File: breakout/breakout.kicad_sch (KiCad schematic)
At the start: 141 parts, among them J1 M20-9982046, J10 B3B-XH-A, J11 B3B-XH-A, J12 B3B-XH-A, J4 B3B-XH-A, J5 B3B-XH-A, J6 B2B-XH-A, J7 B3B-XH-A, J8 B3B-XH-A, J9 B3B-XH-A, Q1 AO3401A, U1 74LVC32APW,118, U10 MCP251863T-E/SS, U11 MCP251863T-E/SS, U12 MCP251863T-E/SS, U13 MCP251863T-E/SS, U14 MCP251863T-E/SS, U15 MCP251863T-E/SS, U16 MCP251863T-E/SS, U2 74LVC04AT14-13, U3 TLV75533PDBVR, U4 74AHC30PW,118, U5 74LVC32APW,118, U9 MCP251863T-E/SS, Y1 ABM8G-40.000MHZ-18-D2Y-T, Y2 ABM8G-40.000MHZ-18-D2Y-T, Y3 ABM8G-40.000MHZ-18-D2Y-T, Y4 ABM8G-40.000MHZ-18-D2Y-T, Y5 ABM8G-40.000MHZ-18-D2Y-T, Y6 ABM8G-40.000MHZ-18-D2Y-T, Y7 ABM8G-40.000MHZ-18-D2Y-T, Y8 ABM8G-40.000MHZ-18-D2Y-T

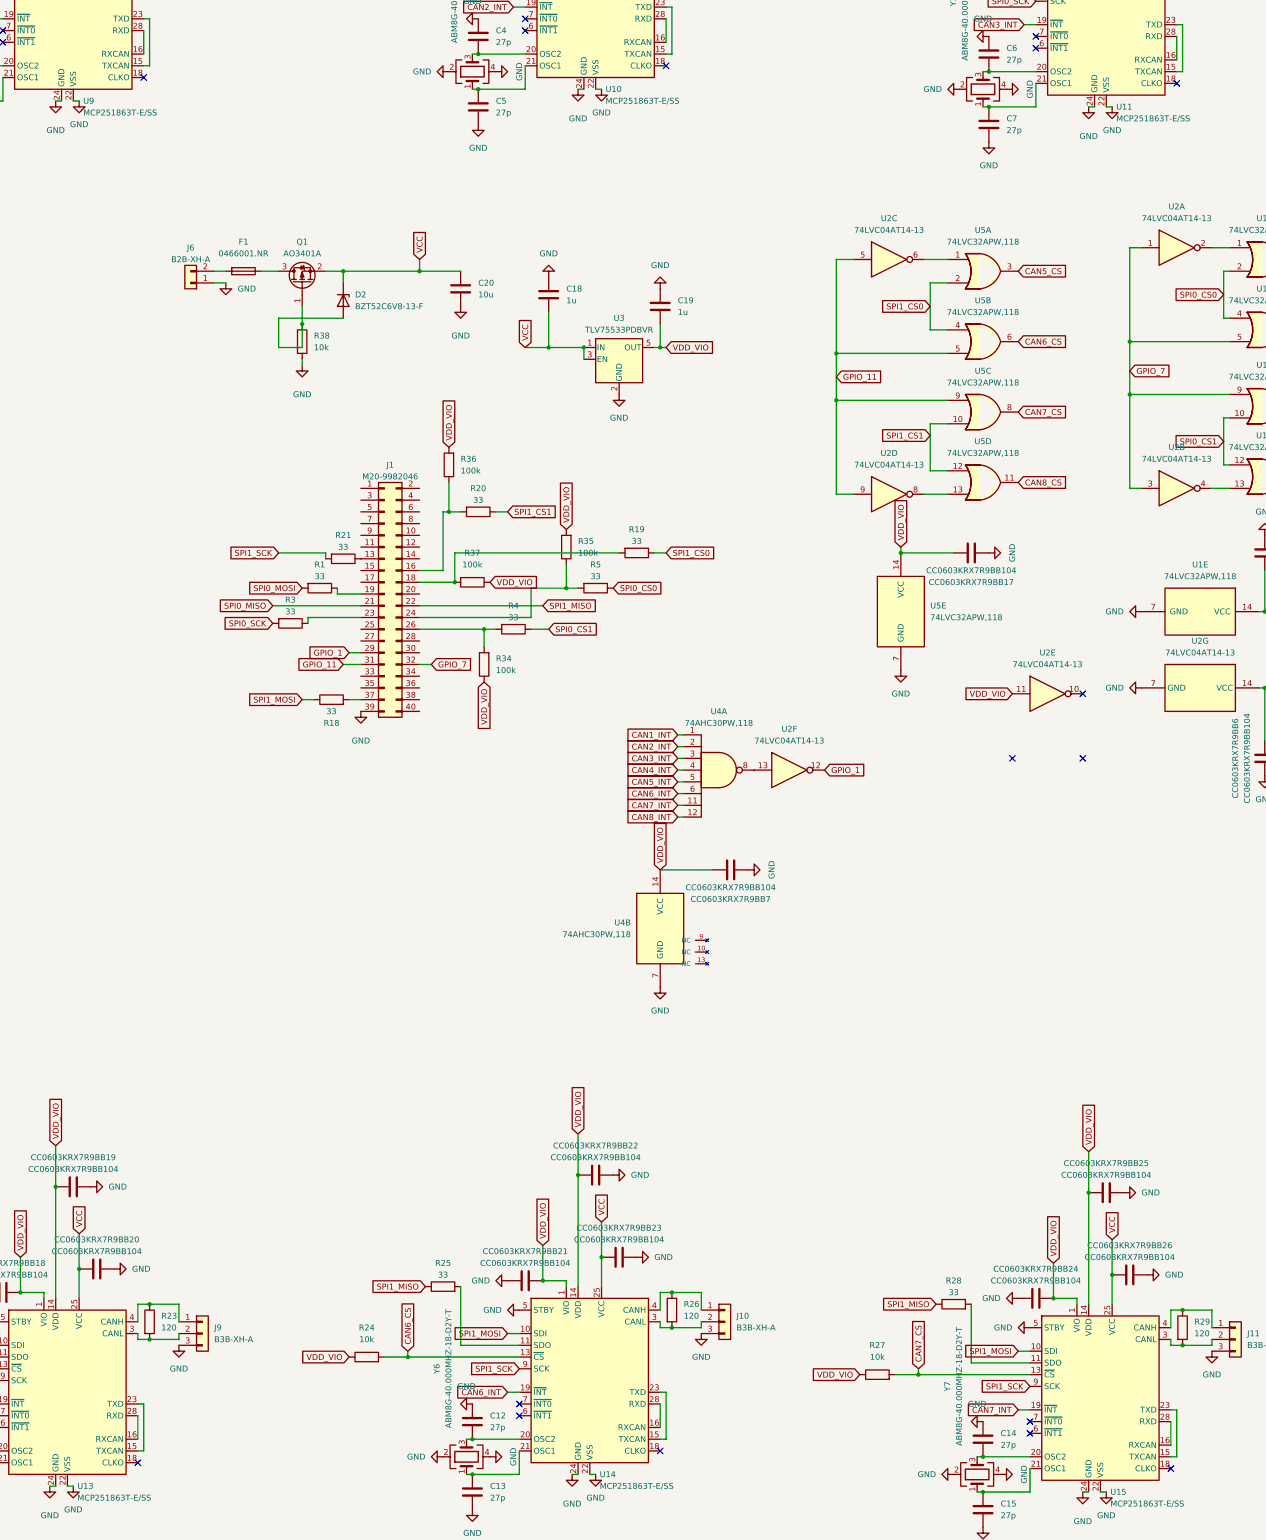
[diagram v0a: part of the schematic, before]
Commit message: Added SMD footprints and started on PCB Layout; currently established 4 PCB layers and started arranging components. Not finished; need to route all components + better organization
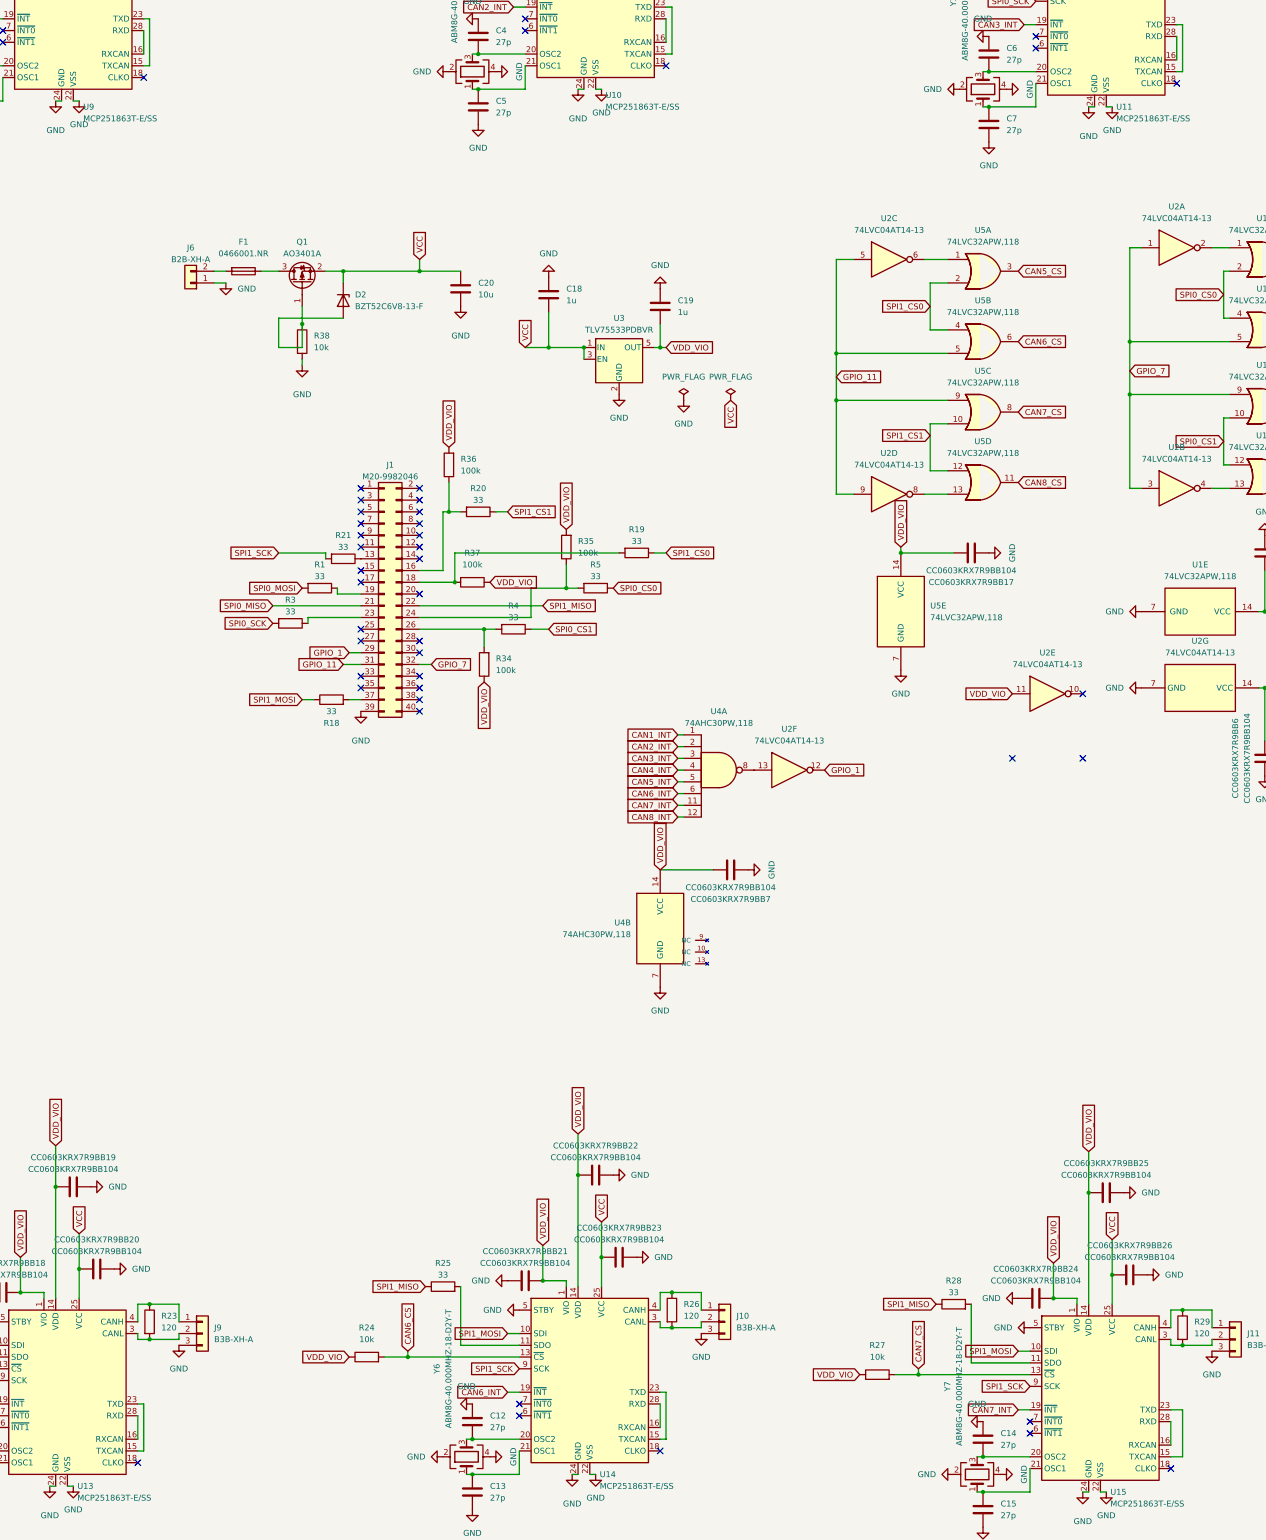
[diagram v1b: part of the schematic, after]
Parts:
- C10, C11, C12, C13, C14, C15, C16, C17, C2, C3, C4, C5, C6, C7, C8, C9: footprint (none) -> Capacitor_SMD:C_0603_1608Metric
- C18, C19: footprint (none) -> BreakoutBoard:C_0603_1608Metric
- C20: footprint (none) -> BreakoutBoard:C_0805_2012Metric
- J1: footprint BreakoutBoard:PinHeader_2x20_P2.54mm_Vertical -> Connector_PinSocket_2.54mm:PinSocket_2x20_P2.54mm_Vertical
- R1, R11, R12, R14, R15, R17, R18, R19, R2, R20, R21, R22, R24, R25, R26, R27, R28, R3, R30, R31, R34, R35, R36, R37, R38, R4, R5, R7, R8, R9: footprint (none) -> BreakoutBoard:R_0603_1608Metric
- R10, R13, R16, R23, R29, R32, R6: footprint (none) -> BreakoutBoard:R_1206_3216Metric
- TP1, TP10, TP11, TP12, TP15, TP16, TP17, TP18, TP19, TP2, TP20, TP21, TP22, TP23, TP3, TP4, TP5, TP6, TP7, TP8, TP9: footprint (none) -> TestPoint:TestPoint_Pad_D1.5mm
- TP13, TP14: footprint (none) -> Connector_PinHeader_2.54mm:PinHeader_1x02_P2.54mm_Vertical
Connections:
- no-connect marks 27 -> 53

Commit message: Complete compact four-layer SPI-to-CAN board layout
Arrange all 141 components on a 77 x 80 mm board, route every connection,
place bypass capacitors beside their IC supply pins, and keep oscillator
signals on the front copper without vias. Shorten SPI clock routes and
document the layer use and route measurements.

Keep schematic/ERC project settings, use portable project library paths,
and remove two stray no-connect markers. Stop tracking KiCad lock files,
local preferences and session history; ignore editor state and backups.

Validation: KiCad 10.0.7 reports zero DRC violations, zero unconnected
items, and zero schematic/PCB parity issues.
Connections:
- no-connect marks 53 -> 51
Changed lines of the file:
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@@
-	)
-	(no_connect
-		(at 196.85 134.62)
 	)
 	(no_connect
@@
 	)
 	(no_connect
-		(at 212.09 134.62)
-	)
-	(no_connect

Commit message: Connect all Jetson J1 ground pins in schematic and PCB
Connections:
- net GND: now also J1.14 (Pin_14), J1.20 (Pin_20), J1.25 (Pin_25), J1.30 (Pin_30), J1.34 (Pin_34), J1.6 (Pin_6), J1.9 (Pin_9)
- no-connect marks 51 -> 44
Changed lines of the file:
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@@
 	)
 	(no_connect
-		(at 55.88 86.36)
-	)
-	(no_connect
 		(at 212.09 120.65)
 	)
@@
 	)
 	(no_connect
-		(at 68.58 99.06)
-	)
-	(no_connect
 		(at 55.88 109.22)
 	)
@@
 	)
 	(no_connect
-		(at 68.58 116.84)
-	)
-	(no_connect
 		(at 303.53 -19.05)
 	)
@@
 	)
 	(no_connect
-		(at 68.58 91.44)
-	)
-	(no_connect
 		(at 201.93 -19.05)
 	)
@@
 	)
 	(no_connect
-		(at 68.58 111.76)
-	)
-	(no_connect
 		(at 8.89 -12.7)
 	)
 	(no_connect
-		(at 68.58 81.28)
-	)
-	(no_connect
 		(at 201.93 -21.59)
 	)
@@
 	)
 	(no_connect
-		(at 55.88 106.68)
-	)
-	(no_connect
 		(at 120.65 284.48)
 	)
@@
 		)
 	)
+	(global_label "GND"
+		(shape input)
+		(at 68.58 81.28 0)
+		(effects (font (size 0.9 0.9)) (justify left))
+	)
+	(global_label "GND"
+		(shape input)
+		(at 55.88 86.36 180)
+		(effects (font (size 0.9 0.9)) (justify right))
+	)
+	(global_label "GND"
+		(shape input)
+		(at 68.58 91.44 0)
+		(effects (font (size 0.9 0.9)) (justify left))
+	)
+	(global_label "GND"
+		(shape input)
+		(at 68.58 99.06 0)
+		(effects (font (size 0.9 0.9)) (justify left))
+	)
+	(global_label "GND"
+		(shape input)
+		(at 55.88 106.68 180)
+		(effects (font (size 0.9 0.9)) (justify right))
+	)
+	(global_label "GND"
+		(shape input)
+		(at 68.58 111.76 0)
+		(effects (font (size 0.9 0.9)) (justify left))
+	)
+	(global_label "GND"
+		(shape input)
+		(at 68.58 116.84 0)
+		(effects (font (size 0.9 0.9)) (justify left))
+	)
 	(symbol
 		(lib_id "Connector:TestPoint")
@@
 		(fields_autoplaced yes)
 		(property "Reference" "R21"
-			(at 52.07 86.36 90)
+			(at 49.53 86.36 90)
 			(show_name no)
 			(do_not_autoplace no)

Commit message: fixed footprints, created orderlist, added mounting holes
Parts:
- C1: renamed from CC0603KRX7R9BB1; value CC0603KRX7R9BB104 -> 100n; MPN (none) -> CC0603KRX7R9BB104; Manufacturer (none) -> YAGEO
- C10, C11, C12, C13, C14, C15, C16, C17, C2, C3, C4, C5, C6, C7, C8, C9: MPN (none) -> CL10C270JB8NNNC; Manufacturer (none) -> Samsung Electro-Mechanics
- C18, C19: MPN (none) -> CGA3E1X7R1E105K080AC; Manufacturer (none) -> TDK
- C20: MPN (none) -> CL21B106KOQNNNE; Manufacturer (none) -> Samsung Electro-Mechanics
- C21: renamed from CC0603KRX7R9BB2; value CC0603KRX7R9BB104 -> 100n; MPN (none) -> CC0603KRX7R9BB104; Manufacturer (none) -> YAGEO
- C22: renamed from CC0603KRX7R9BB3; value CC0603KRX7R9BB104 -> 100n; MPN (none) -> CC0603KRX7R9BB104; Manufacturer (none) -> YAGEO
- C23: renamed from CC0603KRX7R9BB5; value CC0603KRX7R9BB104 -> 100n; MPN (none) -> CC0603KRX7R9BB104; Manufacturer (none) -> YAGEO
- C24: renamed from CC0603KRX7R9BB6; value CC0603KRX7R9BB104 -> 100n; MPN (none) -> CC0603KRX7R9BB104; Manufacturer (none) -> YAGEO
- C25: renamed from CC0603KRX7R9BB7; value CC0603KRX7R9BB104 -> 100n; MPN (none) -> CC0603KRX7R9BB104; Manufacturer (none) -> YAGEO
- C26: renamed from CC0603KRX7R9BB8; value CC0603KRX7R9BB104 -> 100n; MPN (none) -> CC0603KRX7R9BB104; Manufacturer (none) -> YAGEO
- C27: renamed from CC0603KRX7R9BB9; value CC0603KRX7R9BB104 -> 100n; MPN (none) -> CC0603KRX7R9BB104; Manufacturer (none) -> YAGEO
- C28: renamed from CC0603KRX7R9BB10; value CC0603KRX7R9BB104 -> 100n; MPN (none) -> CC0603KRX7R9BB104; Manufacturer (none) -> YAGEO
- C29: renamed from CC0603KRX7R9BB11; value CC0603KRX7R9BB104 -> 100n; MPN (none) -> CC0603KRX7R9BB104; Manufacturer (none) -> YAGEO
- C30: renamed from CC0603KRX7R9BB12; value CC0603KRX7R9BB104 -> 100n; MPN (none) -> CC0603KRX7R9BB104; Manufacturer (none) -> YAGEO
- C31: renamed from CC0603KRX7R9BB13; value CC0603KRX7R9BB104 -> 100n; MPN (none) -> CC0603KRX7R9BB104; Manufacturer (none) -> YAGEO
- C32: renamed from CC0603KRX7R9BB14; value CC0603KRX7R9BB104 -> 100n; MPN (none) -> CC0603KRX7R9BB104; Manufacturer (none) -> YAGEO
- C33: renamed from CC0603KRX7R9BB15; value CC0603KRX7R9BB104 -> 100n; MPN (none) -> CC0603KRX7R9BB104; Manufacturer (none) -> YAGEO
- C34: renamed from CC0603KRX7R9BB16; value CC0603KRX7R9BB104 -> 100n; MPN (none) -> CC0603KRX7R9BB104; Manufacturer (none) -> YAGEO
- C35: renamed from CC0603KRX7R9BB17; value CC0603KRX7R9BB104 -> 100n; MPN (none) -> CC0603KRX7R9BB104; Manufacturer (none) -> YAGEO
- C36: renamed from CC0603KRX7R9BB18; value CC0603KRX7R9BB104 -> 100n; MPN (none) -> CC0603KRX7R9BB104; Manufacturer (none) -> YAGEO
- C37: renamed from CC0603KRX7R9BB19; value CC0603KRX7R9BB104 -> 100n; MPN (none) -> CC0603KRX7R9BB104; Manufacturer (none) -> YAGEO
- C38: renamed from CC0603KRX7R9BB20; value CC0603KRX7R9BB104 -> 100n; MPN (none) -> CC0603KRX7R9BB104; Manufacturer (none) -> YAGEO
- C39: renamed from CC0603KRX7R9BB21; value CC0603KRX7R9BB104 -> 100n; MPN (none) -> CC0603KRX7R9BB104; Manufacturer (none) -> YAGEO
- C40: renamed from CC0603KRX7R9BB22; value CC0603KRX7R9BB104 -> 100n; MPN (none) -> CC0603KRX7R9BB104; Manufacturer (none) -> YAGEO
- C41: renamed from CC0603KRX7R9BB23; value CC0603KRX7R9BB104 -> 100n; MPN (none) -> CC0603KRX7R9BB104; Manufacturer (none) -> YAGEO
- C42: renamed from CC0603KRX7R9BB24; value CC0603KRX7R9BB104 -> 100n; MPN (none) -> CC0603KRX7R9BB104; Manufacturer (none) -> YAGEO
- C43: renamed from CC0603KRX7R9BB25; value CC0603KRX7R9BB104 -> 100n; MPN (none) -> CC0603KRX7R9BB104; Manufacturer (none) -> YAGEO
- C44: renamed from CC0603KRX7R9BB26; value CC0603KRX7R9BB104 -> 100n; MPN (none) -> CC0603KRX7R9BB104; Manufacturer (none) -> YAGEO
- C45: renamed from CC0603KRX7R9BB27; value CC0603KRX7R9BB104 -> 100n; MPN (none) -> CC0603KRX7R9BB104; Manufacturer (none) -> YAGEO
- C46: renamed from CC0603KRX7R9BB28; value CC0603KRX7R9BB104 -> 100n; MPN (none) -> CC0603KRX7R9BB104; Manufacturer (none) -> YAGEO
- C47: renamed from CC0603KRX7R9BB29; value CC0603KRX7R9BB104 -> 100n; MPN (none) -> CC0603KRX7R9BB104; Manufacturer (none) -> YAGEO
- D2: MPN (none) -> BZT52C6V8-13-F; Manufacturer (none) -> Diodes Incorporated
- F1: MPN (none) -> 0466001.NR; Manufacturer (none) -> Littelfuse
- J1: value M20-9982046 -> M20-7832046; symbol BreakoutBoard:M20-9982046 -> BreakoutBoard:M20-7832046; MPN (none) -> M20-7832046; Manufacturer (none) -> Harwin
- J10, J11, J12, J4, J5, J7, J8, J9: MPN (none) -> B3B-XH-A; Manufacturer (none) -> JST
- J6: MPN (none) -> B2B-XH-A; Manufacturer (none) -> JST
- Q1: MPN (none) -> AO3401A; Manufacturer (none) -> Alpha & Omega Semiconductor
- R1, R12, R15, R18, R19, R2, R20, R21, R22, R25, R28, R3, R31, R4, R5, R9: MPN (none) -> RC0603FR-0733RL; Manufacturer (none) -> YAGEO
- R10, R13, R16, R23, R29, R32, R6: MPN (none) -> RC1206FR-07120RL; Manufacturer (none) -> YAGEO
- R11, R14, R17, R24, R27, R30, R38, R7, R8: MPN (none) -> RC0603FR-0710KL; Manufacturer (none) -> YAGEO
- R26: footprint BreakoutBoard:R_0603_1608Metric -> BreakoutBoard:R_1206_3216Metric; MPN (none) -> RC1206FR-07120RL; Manufacturer (none) -> YAGEO
- R34, R35, R36, R37: MPN (none) -> RC0603FR-07100KL; Manufacturer (none) -> YAGEO
- TP13, TP14: value TestPoint_2Pole -> M20-9990246; symbol Connector:TestPoint_2Pole -> BreakoutBoard:M20-9990246; MPN (none) -> M20-9990246; Manufacturer (none) -> Harwin
- U1, U5: MPN (none) -> 74LVC32APW,118; Manufacturer (none) -> Nexperia
- U10, U11, U12, U13, U14, U15, U16, U9: MPN (none) -> MCP251863T-E/SS; Manufacturer (none) -> Microchip
- U2: MPN (none) -> 74LVC04AT14-13; Manufacturer (none) -> Diodes Incorporated
- U3: MPN (none) -> TLV75533PDBVR; Manufacturer (none) -> Texas Instruments
- U4: MPN (none) -> 74AHC30PW,118; Manufacturer (none) -> Nexperia
- Y1, Y2, Y3, Y4, Y5, Y6, Y7, Y8: MPN (none) -> ABM8G-40.000MHZ-18-D2Y-T; Manufacturer (none) -> Abracon
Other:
- moved on the sheet: C1, C10, C11, C12, C13, C14, C15, C16, C17, C18, C19, C2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
